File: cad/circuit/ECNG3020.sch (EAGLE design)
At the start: 27 parts, among them Q1 16Mhz, U1 ATMEGA328P-PU

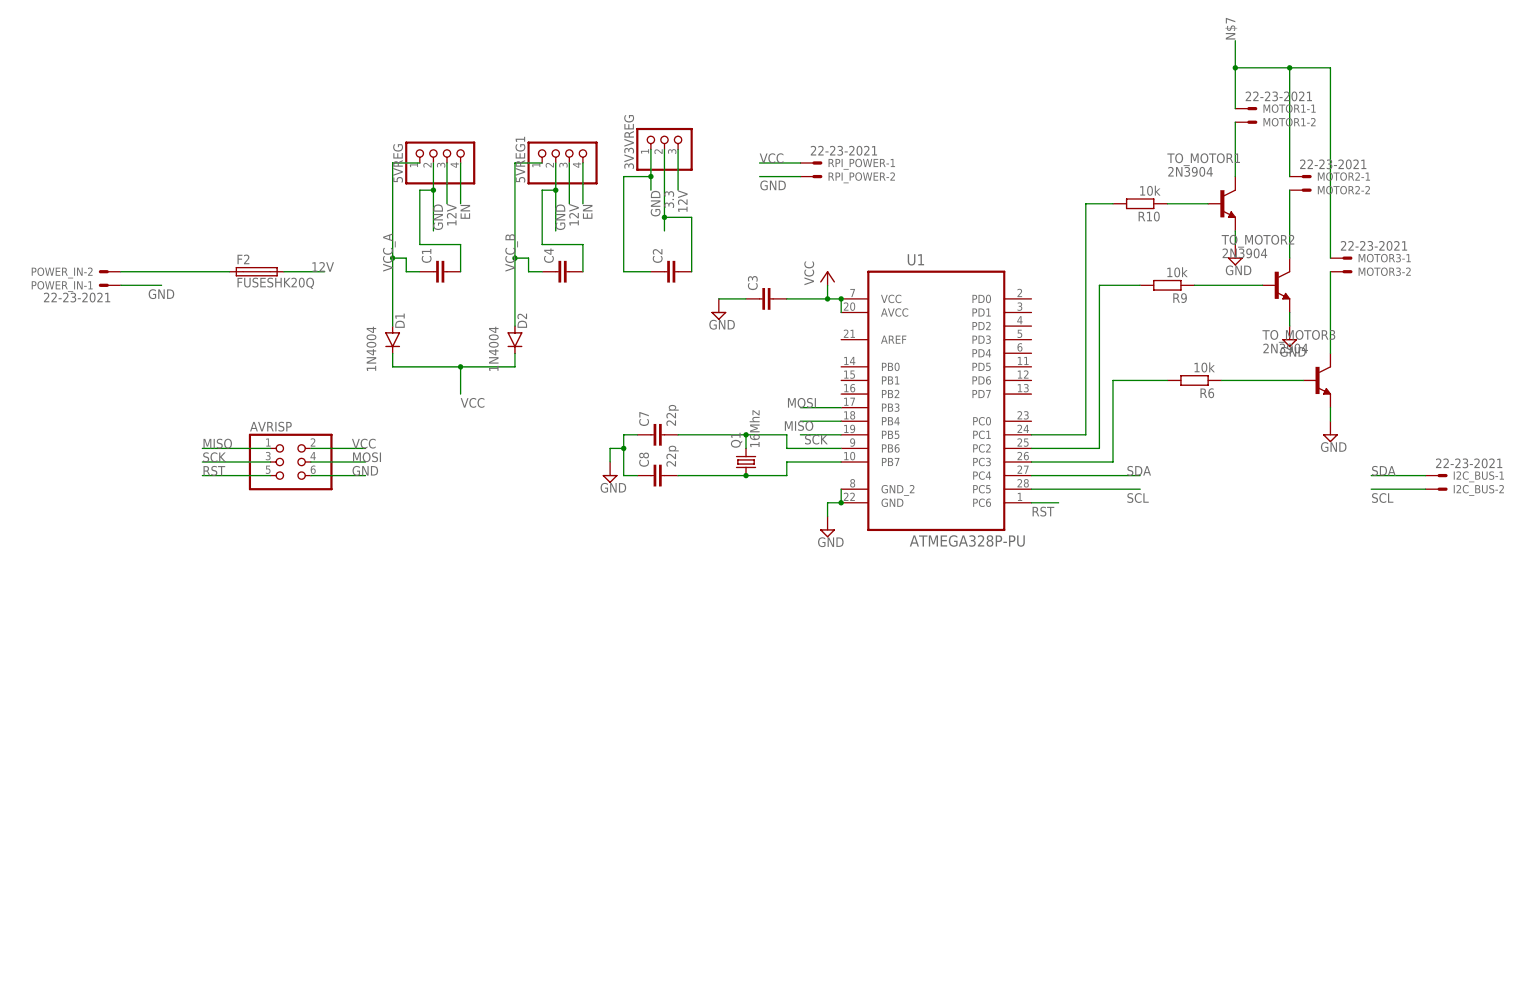
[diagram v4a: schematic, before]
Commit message: Corrected 3.3V connection on PCB
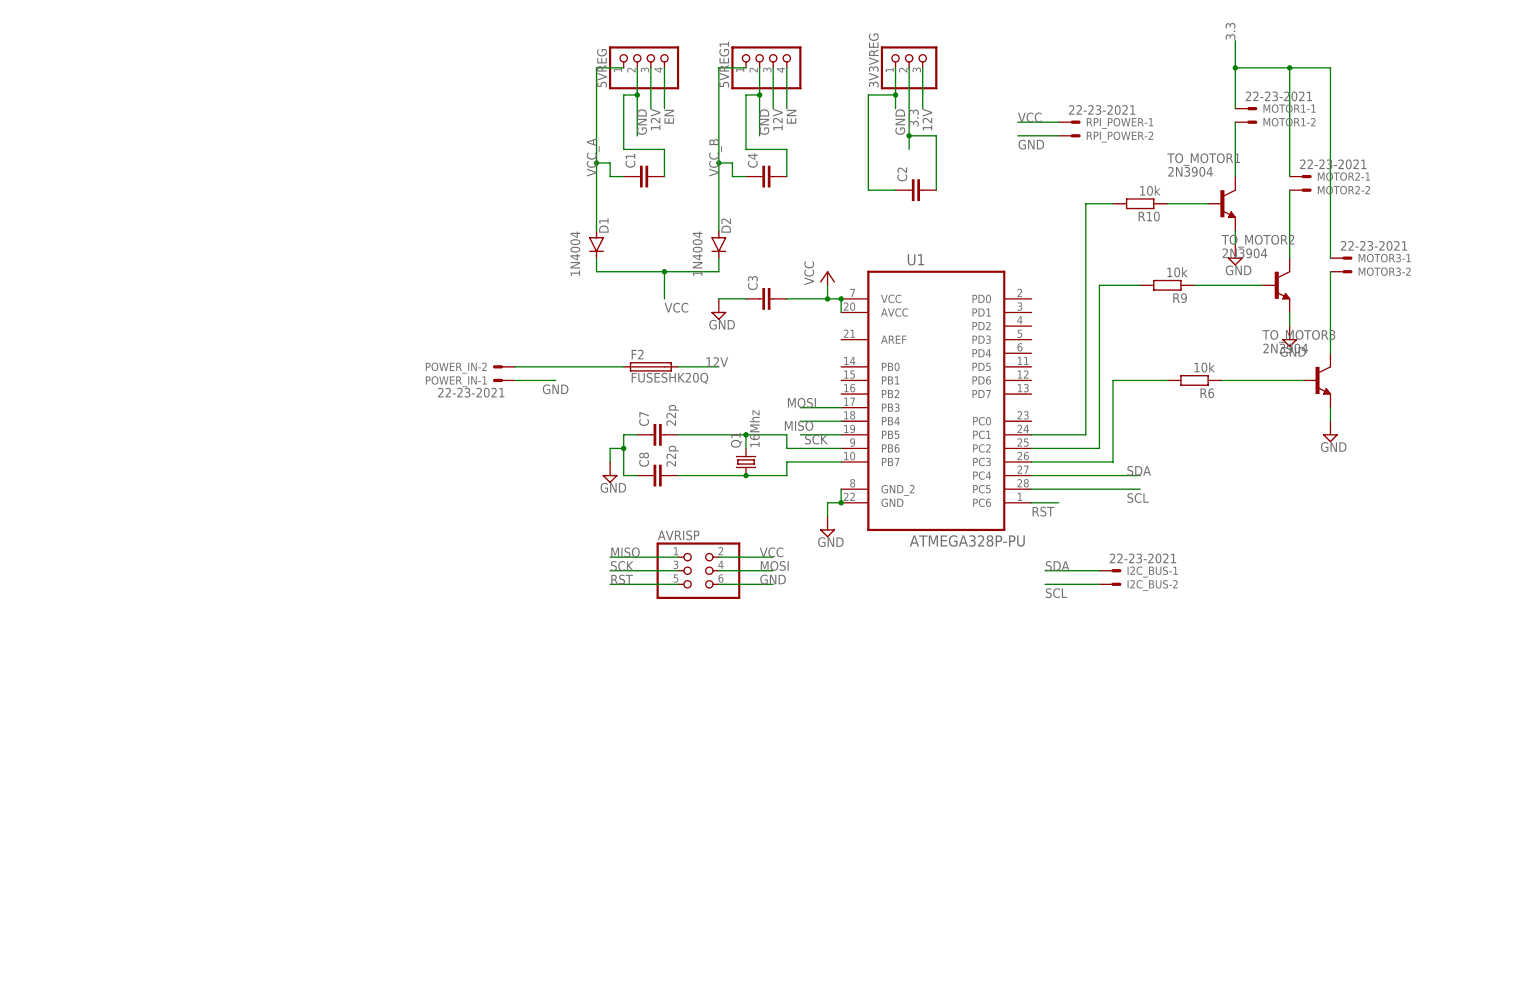
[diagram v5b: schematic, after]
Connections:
- removed net N$7: MOTOR1-1.S, MOTOR2-1.S, MOTOR3-1.S
- net 3.3: now also MOTOR1-1.S, MOTOR2-1.S, MOTOR3-1.S
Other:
- moved on the sheet: 3V3VREG, 5VREG, 5VREG1, AVRISP, C1, C2, C4, D1, D2, F2, I2C_BUS-1, I2C_BUS-2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
